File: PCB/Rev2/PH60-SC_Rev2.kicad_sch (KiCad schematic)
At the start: 43 parts, among them J1 USB_C_Receptacle_USB2.0_14P, J2 Conn_01x02_Pin, J3 Conn_01x02_Pin, U1 nRF52840, X1 32.768kHz, X2 Crystal_Generic

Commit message: Draft commit
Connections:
- no-connect marks 15 -> 23
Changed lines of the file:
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@@
 	)
 	(no_connect
+		(at 256.54 152.4)
+	)
+	(no_connect
 		(at 256.54 200.66)
 	)
 	(no_connect
+		(at 256.54 162.56)
+	)
+	(no_connect
+		(at 256.54 142.24)
+	)
+	(no_connect
 		(at 256.54 193.04)
 	)
@@
 	)
 	(no_connect
+		(at 256.54 137.16)
+	)
+	(no_connect
+		(at 256.54 93.98)
+	)
+	(no_connect
 		(at 256.54 104.14)
 	)
@@
 	)
 	(no_connect
+		(at 256.54 147.32)
+	)
+	(no_connect
 		(at 256.54 127)
 	)
@@
 	)
 	(no_connect
+		(at 256.54 160.02)
+	)
+	(no_connect
 		(at 256.54 111.76)
 	)
+	(no_connect
+		(at 256.54 157.48)
+	)
 	(wire
 		(pts
@@
 		)
 	)
+	(label "VBUS"
+		(at 346.71 184.15 0)
+		(effects
+			(font
+				(size 1.27 1.27)
+			)
+			(justify left bottom)
+		)
+	)
 	(global_label "col_3"
 		(shape input)
@@
 	)
 	(symbol
-		(lib_id "power:PWR_FLAG")
-		(at 350.52 185.42 180)
-		(unit 1)
-		(exclude_from_sim no)
-		(in_bom yes)
-		(on_board yes)
-		(dnp no)
-		(fields_autoplaced yes)
-		(property "Reference" "#FLG01"
-			(at 350.52 187.325 0)
-			(effects
-				(font
-					(size 1.27 1.27)
-				)
-				(hide yes)
-			)
-		)
-		(property "Value" "PWR_FLAG"
-			(at 350.52 190.5 0)
-			(effects
-				(font
-					(size 1.27 1.27)
-				)
-			)
-		)
-		(property "Footprint" ""
-			(at 350.52 185.42 0)
-			(effects
-				(font
-					(size 1.27 1.27)
-				)
-				(hide yes)
-			)
-		)
-		(property "Datasheet" "~"
-			(at 350.52 185.42 0)
-			(effects
-				(font
-					(size 1.27 1.27)
-				)
-				(hide yes)
-			)
-		)
-		(property "Description" "Special symbol for telling ERC where power comes from"
-			(at 350.52 185.42 0)
-			(effects
-				(font
-					(size 1.27 1.27)
-				)
-				(hide yes)
-			)
-		)
-		(pin "1"
-		)
-		(instances
-			(project ""
-				(path "/dca0f898-8fdb-4522-a51d-f4f4238906e7"
-					(reference "#FLG01")
-					(unit 1)
-				)
-			)
-		)
-	)
-	(symbol
 		(lib_id "Device:C_Small")
 		(at 218.44 63.5 0)
@@
 	)
 	(symbol
+		(lib_id "power:VBUS")
+		(at 346.71 184.15 90)
+		(unit 1)
+		(exclude_from_sim no)
+		(in_bom yes)
+		(on_board yes)
+		(dnp no)
+		(fields_autoplaced yes)
+		(property "Reference" "#PWR019"
+			(at 350.52 184.15 0)
+			(effects
+				(font
+					(size 1.27 1.27)
+				)
+				(hide yes)
+			)
+		)
+		(property "Value" "VBUS"
+			(at 342.9 184.1499 90)
+			(effects
+				(font
+					(size 1.27 1.27)
+				)
+				(justify left)
+			)
+		)
+		(property "Footprint" ""
+			(at 346.71 184.15 0)
+			(effects
+				(font
+					(size 1.27 1.27)
+				)
+				(hide yes)
+			)
+		)
+		(property "Datasheet" ""
+			(at 346.71 184.15 0)
+			(effects
+				(font
+					(size 1.27 1.27)
+				)
+				(hide yes)
+			)
+		)
+		(property "Description" "Power symbol creates a global label with name \"VBUS\""
+			(at 346.71 184.15 0)
+			(effects
+				(font
+					(size 1.27 1.27)
+				)
+				(hide yes)
+			)
+		)
+		(pin "1"
+		)
+		(instances
+			(project "PH60-SC_Rev2"
+				(path "/dca0f898-8fdb-4522-a51d-f4f4238906e7"
+					(reference "#PWR019")
+					(unit 1)
+				)
+			)
+		)
+	)
+	(symbol
 		(lib_id "Mechanical:MountingHole")
 		(at 369.57 223.52 0)
@@
 	)
 	(symbol
-		(lib_id "power:VBUS")
-		(at 350.52 185.42 0)
-		(unit 1)
-		(exclude_from_sim no)
-		(in_bom yes)
-		(on_board yes)
-		(dnp no)
-		(fields_autoplaced yes)
-		(property "Reference" "#PWR010"
-			(at 350.52 189.23 0)
-			(effects
-				(font
-					(size 1.27 1.27)
-				)
-				(hide yes)
-			)
-		)
-		(property "Value" "VBUS"
-			(at 350.52 180.34 0)
-			(effects
-				(font
-					(size 1.27 1.27)
-				)
-			)
-		)
-		(property "Footprint" ""
-			(at 350.52 185.42 0)
-			(effects
-				(font
-					(size 1.27 1.27)
-				)
-				(hide yes)
-			)
-		)
-		(property "Datasheet" ""
-			(at 350.52 185.42 0)
-			(effects
-				(font
-					(size 1.27 1.27)
-				)
-				(hide yes)
-			)
-		)
-		(property "Description" "Power symbol creates a global label with name \"VBUS\""
-			(at 350.52 185.42 0)
-			(effects
-				(font
-					(size 1.27 1.27)
-				)
-				(hide yes)
-			)
-		)
-		(pin "1"
-		)
-		(instances
-			(project "PH64lite"
-				(path "/dca0f898-8fdb-4522-a51d-f4f4238906e7"
-					(reference "#PWR010")
-					(unit 1)
-				)
-			)
-		)
-	)
-	(symbol
 		(lib_id "power:PWR_FLAG")
 		(at 384.81 185.42 180)
@@
 					(unit 1)
 				)
+			)
+		)
+	)
+	(symbol
+		(lib_id "power:PWR_FLAG")
+		(at 346.71 184.15 180)
+		(unit 1)
+		(exclude_from_sim no)
+		(in_bom yes)
+		(on_board yes)
+		(dnp no)
+		(fields_autoplaced yes)
+		(property "Reference" "#FLG05"
+			(at 346.71 186.055 0)
+			(effects
+				(font
+					(size 1.27 1.27)
+				)
+				(hide yes)
+			)
+		)
+		(property "Value" "PWR_FLAG"
+			(at 346.71 189.23 0)
+			(effects
+				(font
+					(size 1.27 1.27)
+				)
+			)
+		)
+		(property "Footprint" ""
+			(at 346.71 184.15 0)
+			(effects
+				(font
+					(size 1.27 1.27)
+				)
+				(hide yes)
+			)
+		)
+		(property "Datasheet" "~"
+			(at 346.71 184.15 0)
+			(effects
+				(font
+					(size 1.27 1.27)
+				)
+				(hide yes)
+			)
+		)
+		(property "Description" "Special symbol for telling ERC where power comes from"
+			(at 346.71 184.15 0)
+			(effects
+				(font
+					(size 1.27 1.27)
+				)
+				(hide yes)
+			)
+		)
+		(pin "1"
+		)
+		(instances
+			(project "PH60-SC_Rev2"
+				(path "/dca0f898-8fdb-4522-a51d-f4f4238906e7"
+					(reference "#FLG05")
+					(unit 1)
+				)

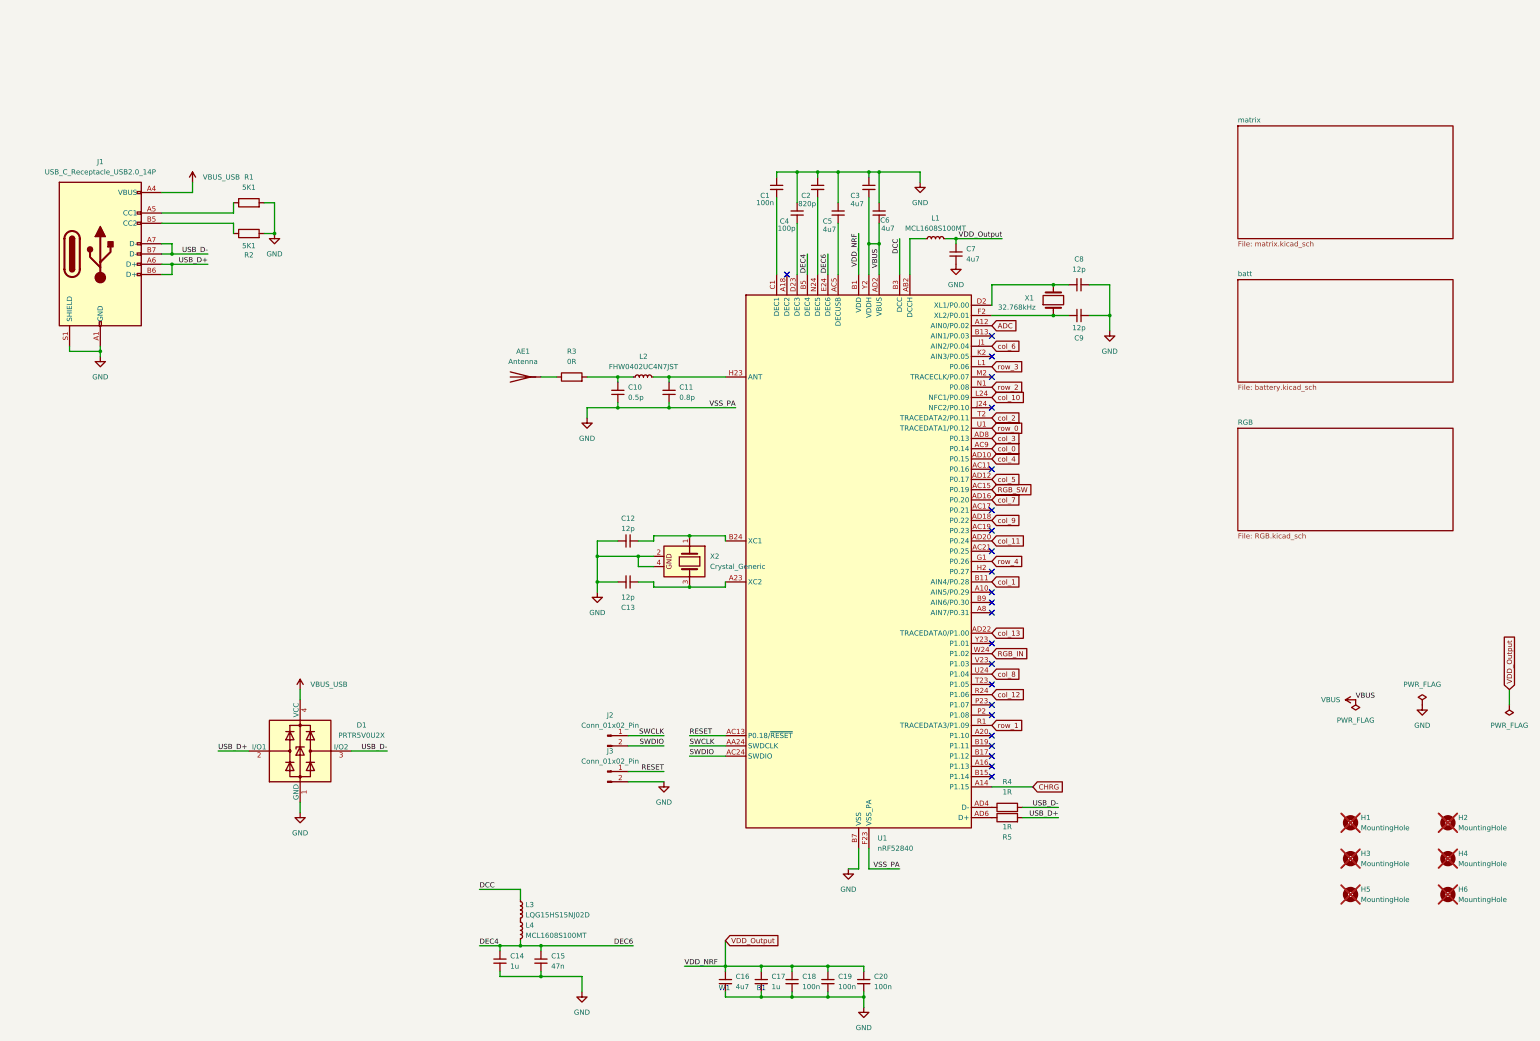
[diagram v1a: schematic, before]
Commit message: Update charger symbol and net
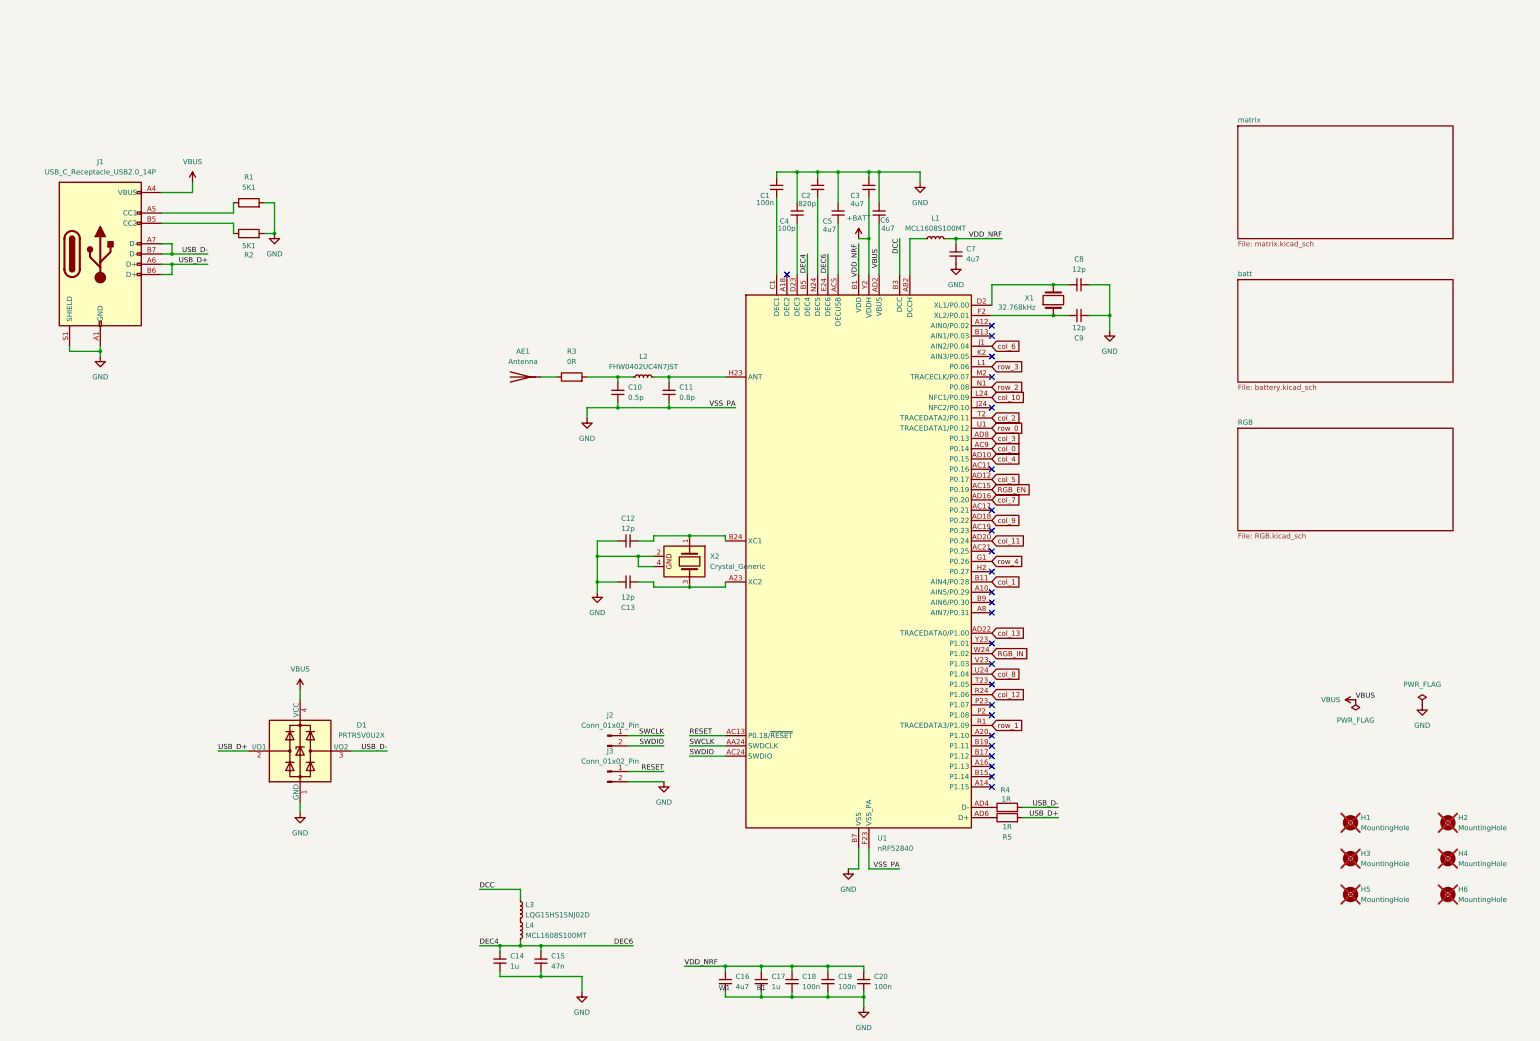
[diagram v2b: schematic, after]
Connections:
- net VBUS_USB is gone; now on net VBUS: D1.4 (VCC), J1.A4 (VBUS), J1.A9 (VBUS), J1.B4 (VBUS), J1.B9 (VBUS)
- net VBUS: no longer C3.2, U1.Y2 (VDDH)
- net ADC: no longer names the net of U1.A12 (AIN0/P0.02)
- net CHRG: no longer names the net of U1.A14 (P1.15)
- net RGB_SW renamed RGB_EN
- net VDD_Output renamed VDD_NRF
- new net +BATT: C3.2, U1.Y2 (VDDH)
- no-connect marks 23 -> 25

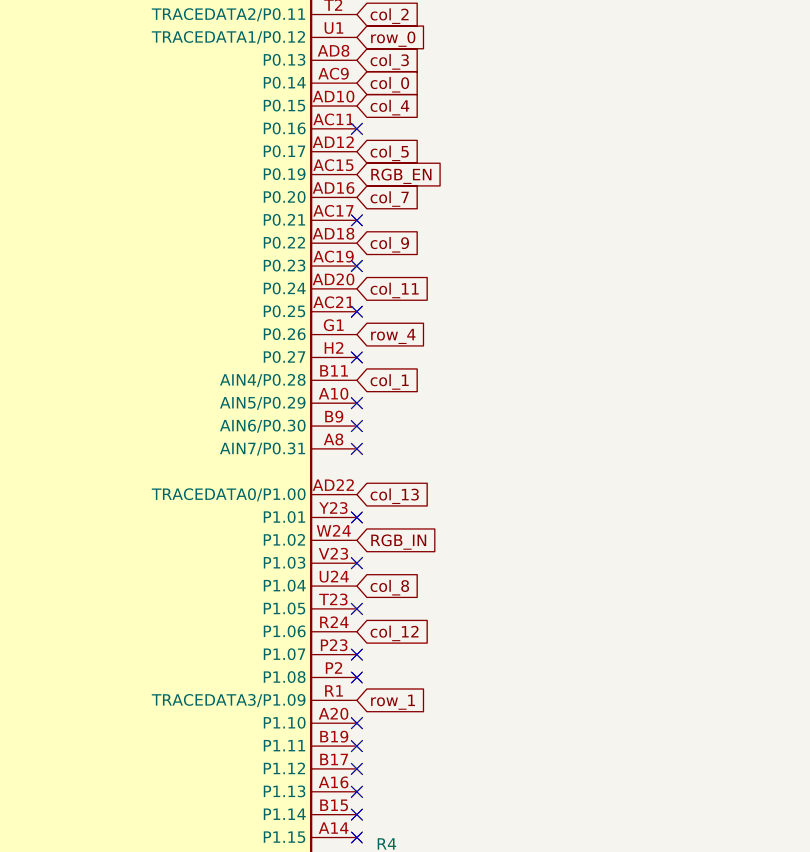
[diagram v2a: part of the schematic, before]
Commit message: 电源芯片布局修改，rgbvdd电源布局修改
待审查，简单drc，电源封装未检查
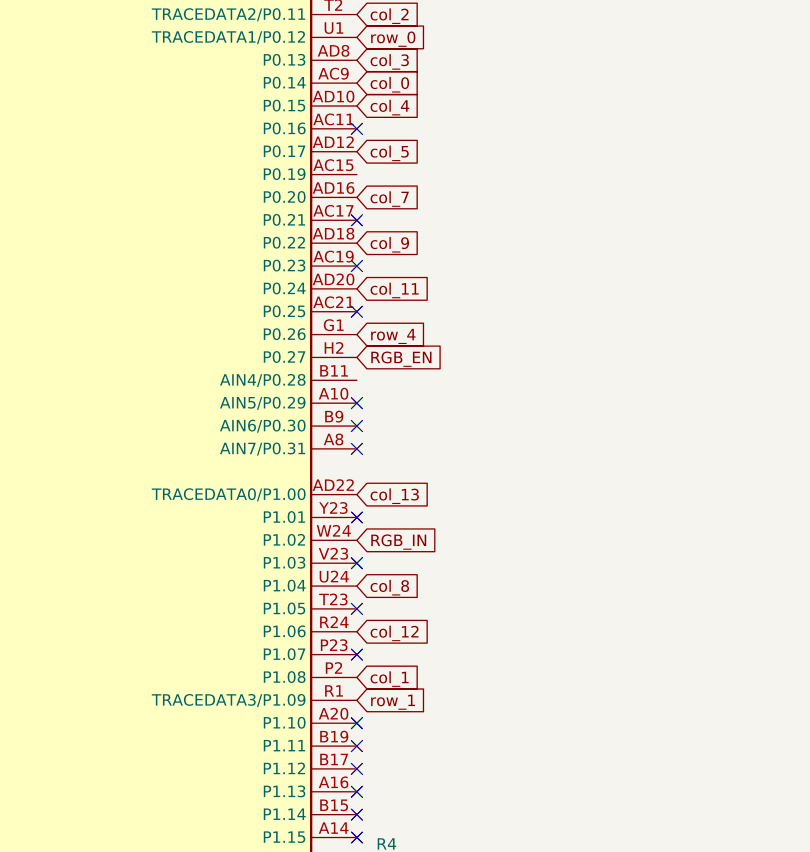
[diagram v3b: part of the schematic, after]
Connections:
- net RGB_EN: now also U1.H2 (P0.27); no longer U1.AC15 (P0.19)
- net col_1: now also U1.P2 (P1.08); no longer U1.B11 (AIN4/P0.28)
- no-connect marks 25 -> 23
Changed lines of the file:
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@@
-	)
-	(no_connect
-		(at 256.54 152.4)
 	)
 	(no_connect
@@
 	(no_connect
 		(at 256.54 198.12)
-	)
-	(no_connect
-		(at 256.54 187.96)
 	)
 	(no_connect
@@
 		)
 	)
+	(global_label "RGB_EN"
+		(shape input)
+		(at 256.54 152.4 0)
+		(fields_autoplaced yes)
+		(effects
+			(font
+				(size 1.27 1.27)
+			)
+			(justify left)
+		)
+		(property "Intersheetrefs" "${INTERSHEET_REFS}"
+			(at 266.7823 152.4 0)
+			(effects
+				(font
+					(size 1.27 1.27)
+				)
+				(justify left)
+				(hide yes)
+			)
+		)
+	)
 	(global_label "col_12"
 		(shape input)
@@
 		)
 	)
-	(global_label "RGB_EN"
-		(shape input)
-		(at 256.54 132.08 0)
-		(fields_autoplaced yes)
-		(effects
-			(font
-				(size 1.27 1.27)
-			)
-			(justify left)
-		)
-		(property "Intersheetrefs" "${INTERSHEET_REFS}"
-			(at 266.7823 132.08 0)
-			(effects
-				(font
-					(size 1.27 1.27)
-				)
-				(justify left)
-				(hide yes)
-			)
-		)
-	)
 	(global_label "row_2"
 		(shape input)
@@
 	(global_label "col_1"
 		(shape input)
-		(at 256.54 154.94 0)
+		(at 256.54 187.96 0)
 		(fields_autoplaced yes)
 		(effects
@@
 		)
 		(property "Intersheetrefs" "${INTERSHEET_REFS}"
-			(at 264.6051 154.94 0)
+			(at 264.6051 187.96 0)
 			(effects
 				(font
